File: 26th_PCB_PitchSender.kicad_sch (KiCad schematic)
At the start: 15 parts, among them J1 Amp, J2 Conn_01x04_Pin, J3 microSD, J4 Conn_01x04_Socket, J5 BNO055, J6 BMP390

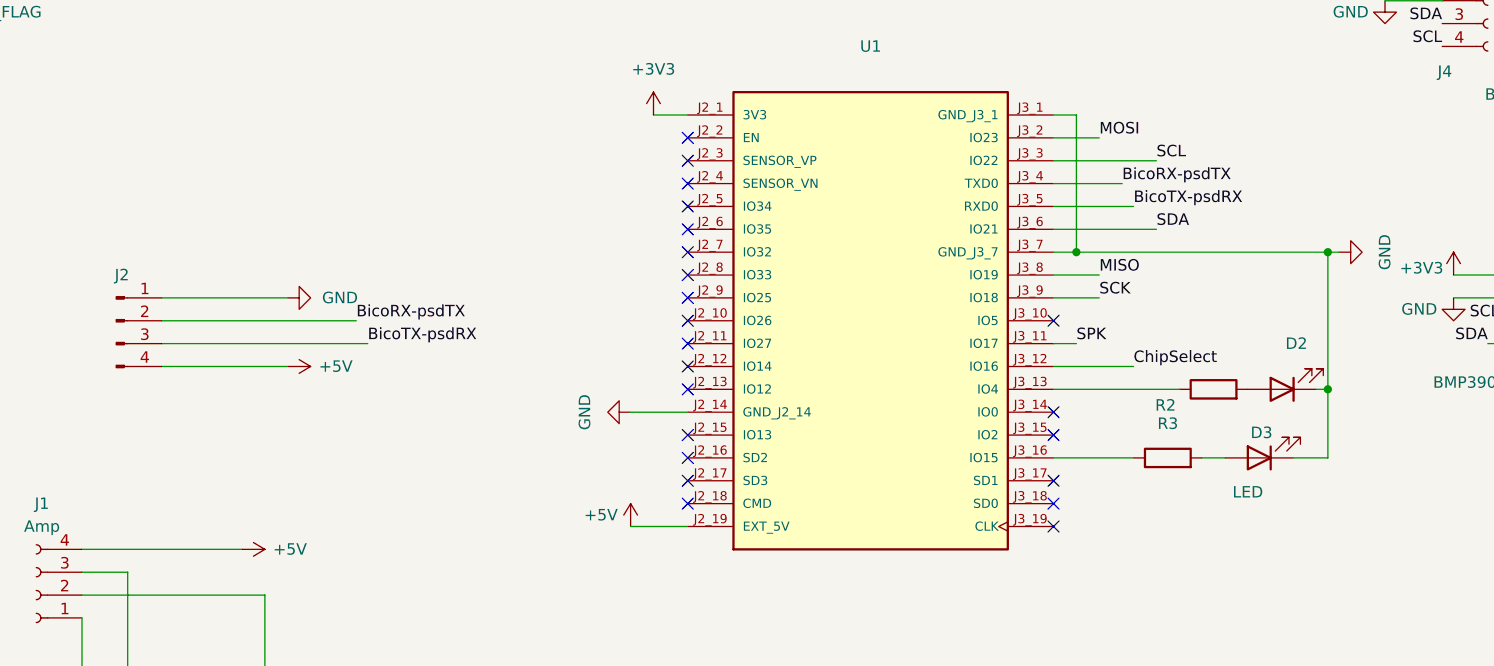
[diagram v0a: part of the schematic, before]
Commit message: UART/LEDピン変更
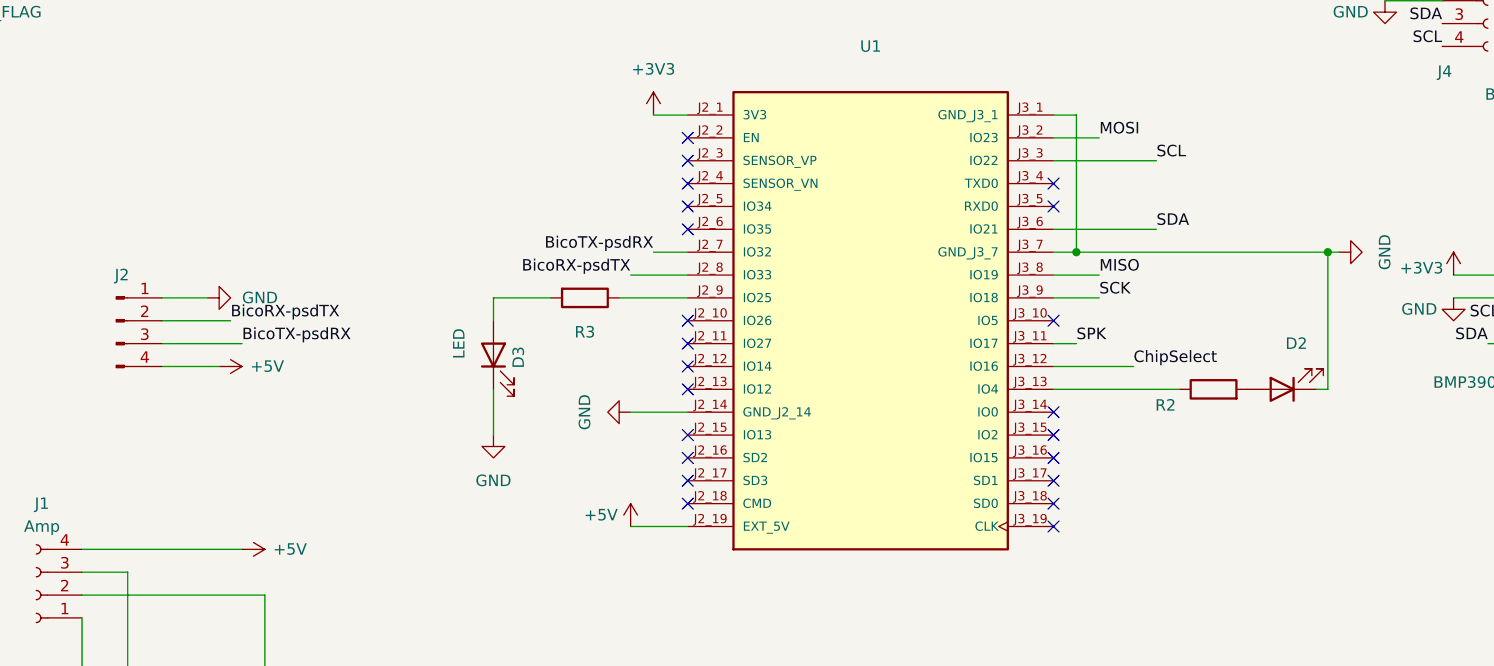
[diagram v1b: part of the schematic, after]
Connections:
- net BicoRX-psdTX: now also U1.J2_8 (IO33); no longer U1.J3_4 (TXD0)
- net BicoTX-psdRX: now also U1.J2_7 (IO32); no longer U1.J3_5 (RXD0)
- net at U1.J2_9 (IO25): now also R3.1
- net at U1.J3_16 (IO15): no longer R3.1
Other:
- moved on the sheet: D3, R3
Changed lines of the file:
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@@
 	)
 	(junction
-		(at 215.9 124.46)
-		(diameter 0)
-		(color 0 0 0 0)
-	)
-	(junction
 		(at 90.17 166.37)
 		(diameter 0)
@@
 	)
 	(no_connect
-		(at 144.78 109.22)
+		(at 185.42 101.6)
 	)
 	(no_connect
@@
 	)
 	(no_connect
-		(at 144.78 99.06)
+		(at 185.42 132.08)
 	)
 	(no_connect
-		(at 144.78 111.76)
+		(at 144.78 99.06)
 	)
 	(no_connect
@@
 	)
 	(no_connect
-		(at 144.78 114.3)
-	)
-	(no_connect
 		(at 185.42 134.62)
 	)
@@
 	)
 	(no_connect
+		(at 185.42 104.14)
+	)
+	(no_connect
 		(at 144.78 104.14)
 	)
@@
 	(wire
 		(pts
-			(xy 215.9 132.08) (xy 212.09 132.08)
+			(xy 82.55 171.45) (xy 82.55 166.37)
 		)
 		(stroke
@@
 	(wire
 		(pts
-			(xy 82.55 171.45) (xy 82.55 166.37)
+			(xy 185.42 114.3) (xy 190.5 114.3)
 		)
 		(stroke
@@
 	(wire
 		(pts
-			(xy 185.42 114.3) (xy 190.5 114.3)
+			(xy 101.6 166.37) (xy 101.6 161.29)
 		)
 		(stroke
@@
 	(wire
 		(pts
-			(xy 101.6 166.37) (xy 101.6 161.29)
+			(xy 82.55 161.29) (xy 82.55 166.37)
 		)
 		(stroke
@@
 	(wire
 		(pts
-			(xy 82.55 161.29) (xy 82.55 166.37)
+			(xy 185.42 121.92) (xy 194.31 121.92)
 		)
 		(stroke
@@
 	(wire
 		(pts
-			(xy 185.42 121.92) (xy 194.31 121.92)
+			(xy 82.55 144.78) (xy 82.55 161.29)
 		)
 		(stroke
@@
 	(wire
 		(pts
-			(xy 82.55 144.78) (xy 82.55 161.29)
+			(xy 123.19 114.3) (xy 129.54 114.3)
 		)
 		(stroke
@@
 	(wire
 		(pts
-			(xy 215.9 132.08) (xy 215.9 124.46)
+			(xy 140.97 109.22) (xy 144.78 109.22)
 		)
 		(stroke
@@
 	(wire
 		(pts
-			(xy 217.17 109.22) (xy 215.9 109.22)
+			(xy 137.16 114.3) (xy 144.78 114.3)
 		)
 		(stroke
@@
 	(wire
 		(pts
-			(xy 234.95 116.84) (xy 236.22 116.84)
+			(xy 217.17 109.22) (xy 215.9 109.22)
 		)
 		(stroke
@@
 	(wire
 		(pts
-			(xy 185.42 132.08) (xy 194.31 132.08)
+			(xy 234.95 116.84) (xy 236.22 116.84)
 		)
 		(stroke
@@
 	(wire
 		(pts
-			(xy 201.93 132.08) (xy 204.47 132.08)
+			(xy 123.19 116.84) (xy 123.19 114.3)
 		)
 		(stroke
@@
 	(wire
 		(pts
-			(xy 86.36 116.84) (xy 107.95 116.84)
+			(xy 86.36 116.84) (xy 93.98 116.84)
 		)
 		(stroke
@@
 	(wire
 		(pts
-			(xy 86.36 114.3) (xy 100.33 114.3)
+			(xy 86.36 114.3) (xy 91.44 114.3)
 		)
 		(stroke
@@
 	(wire
 		(pts
-			(xy 185.42 101.6) (xy 193.04 101.6)
+			(xy 138.43 111.76) (xy 144.78 111.76)
 		)
 		(stroke
@@
 	(wire
 		(pts
-			(xy 86.36 119.38) (xy 109.22 119.38)
+			(xy 86.36 119.38) (xy 95.25 119.38)
 		)
 		(stroke
@@
 	(wire
 		(pts
-			(xy 185.42 104.14) (xy 194.31 104.14)
+			(xy 123.19 124.46) (xy 123.19 129.54)
 		)
 		(stroke
@@
 	(wire
 		(pts
-			(xy 86.36 121.92) (xy 100.33 121.92)
+			(xy 86.36 121.92) (xy 92.71 121.92)
 		)
 		(stroke
@@
 	)
 	(label "BicoTX-psdRX"
-		(at 109.22 119.38 0)
+		(at 95.25 119.38 0)
 		(effects
 			(font
@@
 		)
 	)
-	(label "BicoTX-psdRX"
-		(at 194.31 104.14 0)
-		(effects
-			(font
-				(size 1.27 1.27)
-			)
-			(justify left bottom)
-		)
-	)
 	(label "ChipSelect"
 		(at 73.66 44.45 180)
@@
 	)
 	(label "BicoRX-psdTX"
-		(at 107.95 116.84 0)
+		(at 138.43 111.76 180)
+		(effects
+			(font
+				(size 1.27 1.27)
+			)
+			(justify right bottom)
+		)
+	)
+	(label "BicoRX-psdTX"
+		(at 93.98 116.84 0)
 		(effects
 			(font
@@
 		)
 	)
-	(label "BicoRX-psdTX"
-		(at 193.04 101.6 0)
+	(label "BicoTX-psdRX"
+		(at 140.97 109.22 180)
 		(effects
 			(font
 				(size 1.27 1.27)
 			)
-			(justify left bottom)
+			(justify right bottom)
 		)
 	)
@@
 	(symbol
 		(lib_id "power:+5V")
-		(at 100.33 121.92 270)
+		(at 92.71 121.92 270)
 		(unit 1)
 		(exclude_from_sim no)
@@
 		(dnp no)
 		(property "Reference" "#PWR010"
-			(at 96.52 121.92 0)
+			(at 88.9 121.92 0)
 			(effects
 				(font
@@
 		)
 		(property "Value" "+5V"
-			(at 105.664 121.92 90)
+			(at 98.044 121.92 90)
 			(effects
 				(font
@@
 		)
 		(property "Footprint" ""
-			(at 100.33 121.92 0)
+			(at 92.71 121.92 0)
 			(effects
 				(font
@@
 		)
 		(property "Datasheet" ""
-			(at 100.33 121.92 0)
+			(at 92.71 121.92 0)
 			(effects
 				(font
@@
 		)
 		(property "Description" "Power symbol creates a global label with name \"+5V\""
-			(at 100.33 121.92 0)
+			(at 92.71 121.92 0)
 			(effects
 				(font
@@
 	)
 	(symbol
+		(lib_id "power:GND")
+		(at 123.19 129.54 0)
+		(unit 1)
+		(exclude_from_sim no)
+		(in_bom yes)
+		(on_board yes)
+		(dnp no)
+		(property "Reference" "#PWR019"
+			(at 123.19 135.89 0)
+			(effects
+				(font
+					(size 1.27 1.27)
+				)
+				(hide yes)
+			)
+		)
+		(property "Value" "GND"
+			(at 123.19 134.62 0)
+			(effects
+				(font
+					(size 1.27 1.27)
+				)
+			)
+		)
+		(property "Footprint" ""
+			(at 123.19 129.54 0)
+			(effects
+				(font
+					(size 1.27 1.27)
+				)
+				(hide yes)
+			)
+		)
+		(property "Datasheet" ""
+			(at 123.19 129.54 0)
+			(effects
+				(font
+					(size 1.27 1.27)
+				)
+				(hide yes)
+			)
+		)
+		(property "Description" "Power symbol creates a global label with name \"GND\" , ground"
+			(at 123.19 129.54 0)
+			(effects
+				(font
+					(size 1.27 1.27)
+				)
+				(hide yes)
+			)
+		)
+		(pin "1"
+		)
+		(instances
+			(project "26th_PCB_PitchSender"
+				(path "/5013cac2-53c1-4b5b-9014-63fb93daa52f"
+					(reference "#PWR019")
+					(unit 1)
+				)
+			)
+		)
+	)
+	(symbol
 		(lib_id "Device:LED")
-		(at 208.28 132.08 180)
+		(at 123.19 120.65 90)
 		(unit 1)
 		(exclude_from_sim no)
@@
 		(dnp no)
 		(property "Reference" "D3"
-			(at 208.534 129.286 0)
+			(at 125.984 120.904 0)
 			(effects
 				(font
@@
 		)
 		(property "Value" "LED"
-			(at 207.01 135.89 0)
+			(at 119.38 119.38 0)
 			(effects
 				(font
@@
 		)
 		(property "Footprint" "LED_THT:LED_D3.0mm"
-			(at 208.28 132.08 0)
+			(at 123.19 120.65 0)
 			(effects
 				(font
@@
 		)
 		(property "Datasheet" "~"
-			(at 208.28 132.08 0)
+			(at 123.19 120.65 0)
 			(effects
 				(font
@@
 		)
 		(property "Description" "Light emitting diode"
-			(at 208.28 132.08 0)
+			(at 123.19 120.65 0)
 			(effects
 				(font
@@
 		)
 		(property "Sim.Pins" "1=K 2=A"
-			(at 208.28 132.08 0)
+			(at 123.19 120.65 0)
 			(effects
 				(font
@@
 	(symbol
 		(lib_id "Device:R")
-		(at 198.12 132.08 90)
+		(at 133.35 114.3 270)
 		(unit 1)
 		(exclude_from_sim no)
@@
 		(fields_autoplaced yes)
 		(property "Reference" "R3"
-			(at 198.12 128.27 90)
+			(at 133.35 118.11 90)
 			(effects
 				(font
@@
 		)
 		(property "Value" "R"
-			(at 198.12 128.27 90)
+			(at 133.35 118.11 90)
 			(effects
 				(font
@@
 		)
 		(property "Footprint" "Resistor_THT:R_Axial_DIN0204_L3.6mm_D1.6mm_P5.08mm_Horizontal"
-			(at 198.12 133.858 90)
+			(at 133.35 112.522 90)
 			(effects
 				(font
@@
 		)
 		(property "Datasheet" "~"
-			(at 198.12 132.08 0)
+			(at 133.35 114.3 0)
 			(effects
 				(font
@@
 		)
 		(property "Description" "Resistor"
-			(at 198.12 132.08 0)
+			(at 133.35 114.3 0)
 			(effects
 				(font
@@
 	(symbol
 		(lib_id "power:GND")
-		(at 100.33 114.3 90)
+		(at 91.44 114.3 90)
 		(unit 1)
 		(exclude_from_sim no)
@@
 		(fields_autoplaced yes)
 		(property "Reference" "#PWR09"
-			(at 106.68 114.3 0)
+			(at 97.79 114.3 0)
 			(effects
 				(font
@@
 		)
 		(property "Value" "GND"
-			(at 104.14 114.2999 90)
+			(at 95.25 114.2999 90)
 			(effects
 				(font
@@
 		)
 		(property "Footprint" ""
-			(at 100.33 114.3 0)
+			(at 91.44 114.3 0)
 			(effects
 				(font
@@
 		)
 		(property "Datasheet" ""
-			(at 100.33 114.3 0)
+			(at 91.44 114.3 0)
 			(effects
 				(font
@@
 		)
 		(property "Description" "Power symbol creates a global label with name \"GND\" , ground"
-			(at 100.33 114.3 0)
+			(at 91.44 114.3 0)
 			(effects
 				(font
